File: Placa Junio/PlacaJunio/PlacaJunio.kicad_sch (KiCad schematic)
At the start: 13 parts, among them IC1 LC86LICMD, J1 Bateria, Q4 IRLML0030, U4 MODULO MICRO SD, U5 TSR2-2433N

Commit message: .
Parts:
- removed U4: MODULO MICRO SD, symbol _mio:MODULO_MICROSD
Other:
- added sheet MicroSD (MicroSD.kicad_sch)
- note removed: "Memoria"

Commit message: Esquemático Completo
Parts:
- U1: footprint (none) -> Cohete_Julio:Nano BLE 33 Sense
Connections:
- net +3V3: now also IC1.5 (V_BCKP)
- no-connect marks 16 -> 15
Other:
- note added: "Control Cargas pólvora"
- note added: "Memoria"
- moved on the sheet: BZ1, C2, C5, C6, C7, IC1, J1, Q4, R9, U3, U5

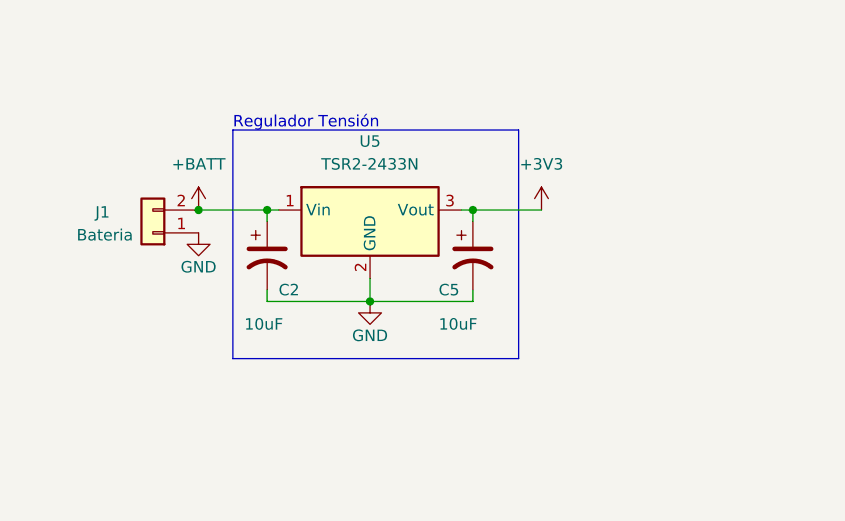
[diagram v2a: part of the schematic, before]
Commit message: Elementos posicionados
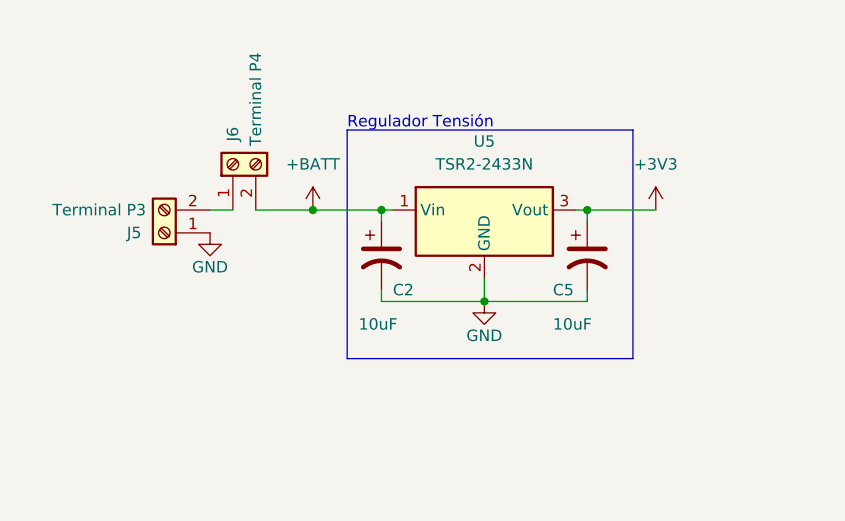
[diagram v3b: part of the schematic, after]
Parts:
- removed J1: Bateria, Connector_JST:JST_PH_B2B-PH-K_1x02_P2.00mm_Vertical, symbol Connector_Generic:Conn_01x02
- added J5: Terminal P3, TerminalBlock:TerminalBlock_bornier-2_P5.08mm, symbol Connector:Screw_Terminal_01x02
- added J6: Terminal P4, TerminalBlock:TerminalBlock_bornier-2_P5.08mm, symbol Connector:Screw_Terminal_01x02
- BZ1: footprint Buzzer_Beeper:Buzzer_TDK_PS1240P02BT_D12.2mm_H6.5mm -> Buzzer_Beeper:MagneticBuzzer_CUI_CMT-8504-100-SMT
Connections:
- net +BATT: now also J6.2 (Pin_2)
- net GND: now also J5.1 (Pin_1)
- new net: J5.2 (Pin_2), J6.1 (Pin_1)
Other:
- moved on the sheet: C2, C5, U5
